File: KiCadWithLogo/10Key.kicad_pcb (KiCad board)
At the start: 2 copper layers, 73 x 102.5 mm, 61 parts, among them P1 USB_OTG, P2 Program, Q1 MMBT3906, Q2 MMBT3906, Q3 MMBT3906, Q4 MMBT3906, Q5 MMBT3906, SW1 SW_PUSH, SW10 5, SW11 2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

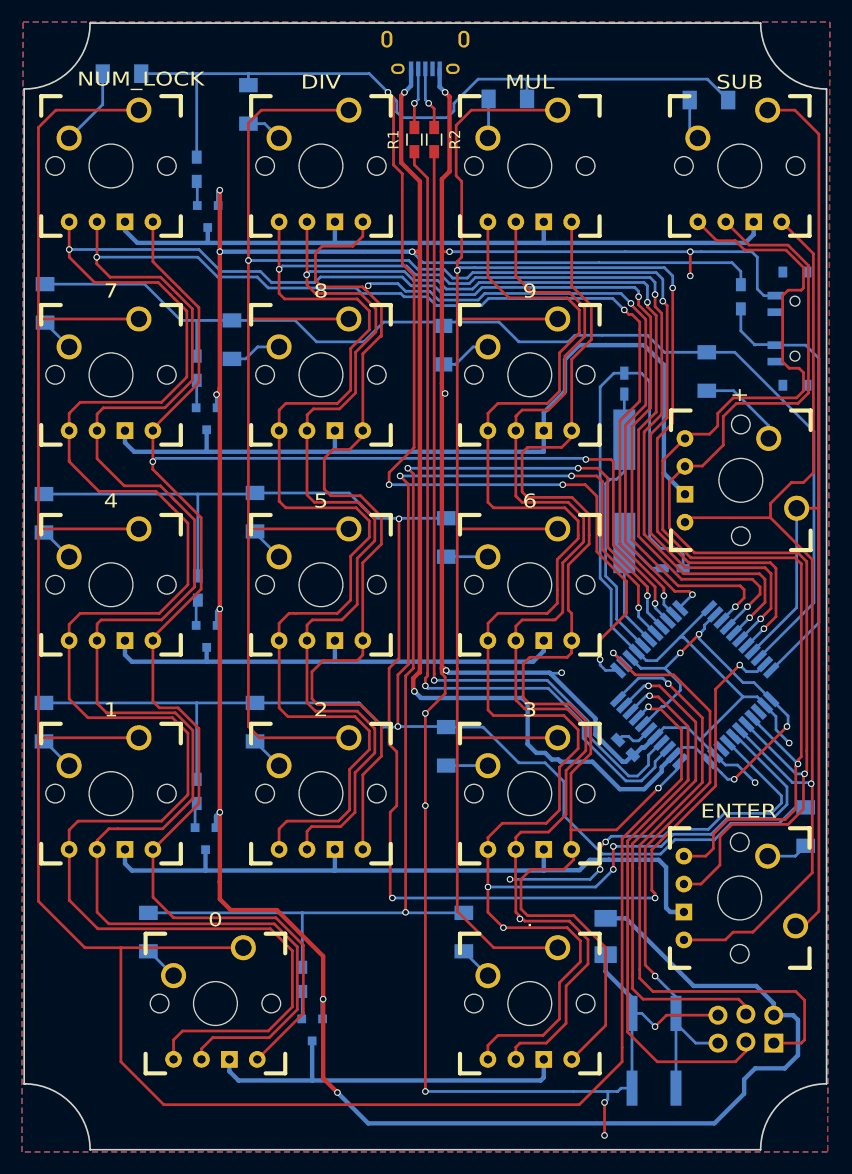
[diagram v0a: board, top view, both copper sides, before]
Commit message: * Added extra capacitance * Added current limiting resistors * Moved connections off of the jtag pins so that an external programmer * will not be needed to set fuses.
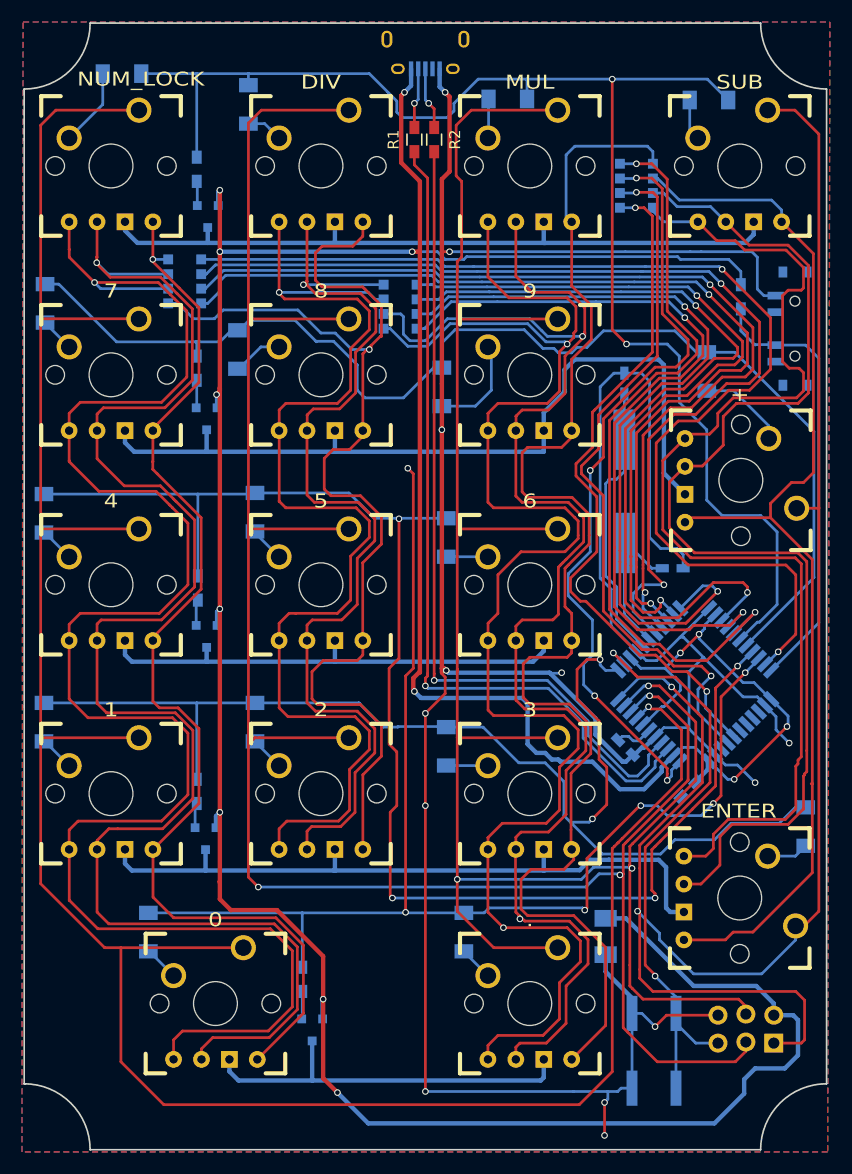
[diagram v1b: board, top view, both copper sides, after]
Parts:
- added C5: 0.1uF, Capacitors_SMD:C_0603_HandSoldering, B.Cu at (170.9, 118.2)
- added RP1: 100, Resistors_SMD:R_Array_Convex_4x1206, B.Cu at (125.1, 72.0)
- added RP2: 100, Resistors_SMD:R_Array_Convex_4x1206, B.Cu at (144.7, 74.3)
- added RP3: 100, Resistors_SMD:R_Array_Convex_4x1206, B.Cu at (166.2, 63.3)
- moved D11 3.80 mm to (148.5, 81.6)
- moved D7 1.03 mm to (129.9, 78.2)
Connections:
- P2 pad 1: /MISO -> /COL3
- P2 pad 3: /SCK -> /COL1
- P2 pad 4: /MOSI -> /COL2
- U1 pad 1: /LEDR2 -> Net-(RP3-Pad3)
- U1 pad 10: /MOSI -> /COL2
- U1 pad 11: /MISO -> /COL3
- U1 pad 12: /ROW0 -> /ROW3
- U1 pad 18: /ROW3 -> Net-(RP1-Pad2)
- U1 pad 19: /ROW4 -> Net-(RP1-Pad3)
- U1 pad 20: /LEDR0 -> Net-(RP1-Pad4)
- U1 pad 21: /LEDG0 -> Net-(RP2-Pad1)
- U1 pad 22: /LEDR1 -> Net-(RP2-Pad3)
- U1 pad 25: /LEDB0 -> Net-(RP2-Pad2)
- U1 pad 26: /LEDG1 -> Net-(RP2-Pad4)
- U1 pad 27: /LEDB1 -> Net-(RP3-Pad4)
- U1 pad 28: /COL1 -> /ROW0
- U1 pad 29: /COL2 -> /ROW1
- U1 pad 30: /COL3 -> /ROW2
- U1 pad 31: /ROW1 -> /ROW4
- U1 pad 32: /ROW2 -> Net-(RP1-Pad1)
- U1 pad 37: /LEDB3 -> Net-(U1-Pad37)
- U1 pad 38: /LEDG3 -> Net-(U1-Pad38)
- U1 pad 39: /LEDR3 -> Net-(U1-Pad39)
- U1 pad 40: /LEDB2 -> Net-(RP3-Pad1)
- U1 pad 41: /LEDG2 -> Net-(RP3-Pad2)
- U1 pad 9: /SCK -> /COL1
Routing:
- net Net-(RP1-Pad1): track 0.00 -> 103.7 mm, vias 0 -> 2
- net Net-(RP1-Pad2): track 0.00 -> 92.0 mm, vias 0 -> 2
- net Net-(RP1-Pad4): track 0.00 -> 87.7 mm, vias 0 -> 2
- net Net-(RP1-Pad3): track 0.00 -> 87.7 mm, vias 0 -> 2
- net /LEDB0: track 247.5 -> 160.5 mm, vias 3 -> 1
- net Net-(RP2-Pad2): track 0.00 -> 78.3 mm, vias 0 -> 2
- net /LEDG0: track 220.5 -> 145.6 mm, vias 3 -> 1
- net Net-(RP2-Pad3): track 0.00 -> 73.2 mm, vias 0 -> 2
- net Net-(RP2-Pad4): track 0.00 -> 72.7 mm, vias 0 -> 2
- net Net-(RP3-Pad3): track 0.00 -> 71.8 mm, vias 0 -> 4
- net Net-(RP3-Pad4): track 0.00 -> 69.3 mm, vias 0 -> 2
- net /LEDB1: track 174.8 -> 106.6 mm, vias 3 -> 1
- net Net-(RP2-Pad1): track 0.00 -> 67.5 mm, vias 0 -> 2
- net /LEDG1: track 157.8 -> 91.8 mm, vias 3 -> 1
- net Net-(RP3-Pad2): track 0.00 -> 65.0 mm, vias 0 -> 2
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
